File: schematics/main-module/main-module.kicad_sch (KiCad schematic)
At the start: 68 parts, among them J1 Conn_01x02_Socket, J3 Conn_01x04_Socket, J3 USB_C_Receptacle_USB2.0, J4 Conn_01x04_Pin, J5 Conn_01x02_Socket, J6 Conn_01x02_Pin, J7 FS1000A@433Mhz, J8 XY-MK-5V@433MHz, J9 AU-RM-5V@315мГц, M1 Creality 42-40, Q14 IRLML0030, Q7 BC847, SW1 KLS7-TS6601-7.0-180, SW2 SW_Push, U19 INA169, U2 CP2102N-Axx-xQFN28, U3 TMC2209_Module, U4 AMS1117-3.3, U8 ESP32-WROOM-32

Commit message: Creating schematics and boards
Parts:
- removed C18: 10 nF, Capacitor_SMD:C_0603_1608Metric, symbol Device:C
- removed C25 (x2): ?, Capacitor_SMD:C_0603_1608Metric, symbol Device:C
- removed J5: Conn_01x02_Socket, symbol Connector:Conn_01x02_Socket
- removed Q14 (x2): IRLML0030, Package_TO_SOT_SMD:SOT-23, symbol Transistor_FET:IRLML0030
- removed R15 (x2): 10K, Resistor_SMD:R_0805_2012Metric, symbol Device:R
- removed R52: 0.01, Resistor_SMD:R_2512_6332Metric, symbol Device:R
- removed R53: ?, Resistor_SMD:R_0805_2012Metric, symbol Device:R
- removed U19: INA169, Package_TO_SOT_SMD:SOT-23-5, symbol Amplifier_Current:INA169
- added C1: 1 uF, Capacitor_SMD:C_0603_1608Metric, symbol Device:C
- added C10 (x2): 1000 uF, symbol Device:C_Polarized
- added C10: 100 uF, symbol Device:C_Polarized
- added C11: 1000 uF, Capacitor_THT:CP_Radial_D8.0mm_P3.50mm, symbol Device:C_Polarized
- added C19 (x4): 22 uF, Capacitor_SMD:C_1210_3225Metric, symbol Device:C
- added C2: 400 pF, Capacitor_SMD:C_0603_1608Metric, symbol Device:C
- added C25: 1 nF, Capacitor_SMD:C_0603_1608Metric, symbol Device:C
- added C25: 10 uF, Capacitor_SMD:C_0603_1608Metric, symbol Device:C
- added C25: 500 nF, Capacitor_SMD:C_0603_1608Metric, symbol Device:C
- added C25 (x2), C26: 100 nF, Capacitor_SMD:C_0603_1608Metric, symbol Device:C
- added D2: HER508, Diode_THT:D_DO-201AD_P3.81mm_Vertical_AnodeUp, symbol Device:D
- added D3: US1M, Diode_SMD:D_SMA, symbol Device:D
- added D7: MB10S, Library:MBS, symbol Device:D_Bridge_+-AA
- added F1: 5A, symbol Device:Fuse
- added F1: 3A, symbol Device:Fuse
- added J3: Charger, symbol Connector:Conn_01x02_Socket
- added JP1: Charge from flusher, Library:SolderedJumper-2P-2mm, symbol Jumper:SolderJumper_2_Open
- added NT1: AGND/PGND, symbol Device:NetTie_2
- added Q1 (x2): IRF7832PbF, Package_SO:SOIC-8_3.9x4.9mm_P1.27mm, symbol Transistor_FET:IRF7403
- added Q14 (x2): IRLML0030, Package_TO_SOT_SMD:SOT-23, symbol Transistor_FET:IRLML0030
- added Q4: IRF7425PbF, Package_SO:SOIC-8_3.9x4.9mm_P1.27mm, symbol Transistor_FET:IRF7404
- added Q9: IRLML5203, Package_TO_SOT_SMD:SOT-23, symbol Transistor_FET:IRLML5203
- added R15 (x5): 10K, Resistor_SMD:R_0805_2012Metric, symbol Device:R
- added R15 (x4): 1K, Resistor_SMD:R_0805_2012Metric, symbol Device:R
- added R6: 50, 1W, symbol Device:R
- added RV1: 30K, symbol Device:R_Potentiometer
- added RV2: 1K, symbol Device:R_Potentiometer
- added T1: Transformer_1P_SS, symbol Device:Transformer_1P_SS
- added TP1, TP4: GND, symbol Connector:TestPoint
- added TP2: +5V, symbol Connector:TestPoint
- added TP3: +3V3, symbol Connector:TestPoint
- added TP5: VREF, symbol Connector:TestPoint
- added U3: AMS1117-5.0, Package_TO_SOT_SMD:SOT-223-3_TabPin2, symbol Regulator_Linear:AMS1117-5.0
- added U3: MC34063AD, Package_SO:SOP-8_3.9x4.9mm_P1.27mm, symbol Regulator_Switching:MC34063AD
- added U6: TL494, symbol Regulator_Controller:TL494
- added U7, U8: FAN3100, Package_TO_SOT_SMD:SOT-23-5, symbol My_Library:FAN3100
- J4: renamed from J7; value FS1000A@433Mhz -> STX882@433Mhz
- J5: renamed from J8; value XY-MK-5V@433MHz -> SRX882@433MHz
- J6: value Conn_01x02_Pin -> Power; now fitted
- L1: value L -> AMPLF0630, 8,2uH; now fitted
- R15: value 10K -> 1K
- renumbered D4 to D6, J9 to J7, J3 to J8, J4 to J9, U3 to U9
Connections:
- net +3V3: now also R15.1, TP3.1
- net +5V: now also C19.2, D3.1 (K), TP2.1, U3.2 (VO); no longer C10.1, C10.1, C19.2, C19.2, C29.1, C33.1, D5.2 (A2), J1.2 (Pin_2), J3.A4 (VBUS), J3.A9 (VBUS), J3.B4 (VBUS), J3.B9 (VBUS), R15.1, R15.1, U9.9 (VM)
- net GND1: now reaches D6.1 (K)
- net GND1: now also J6.2 (Pin_2), C10.2, C19.1, C19.1, C25.2, C25.2, C25.2, C25.2, D7.2 (-), Q1.1 (S), Q1.1 (S), Q1.2 (S), Q1.2 (S), Q1.3 (S), Q1.3 (S), R15.2, R15.2, RV2.3, TP4.1, U6.1 (1IN+), U6.10 (E2), U6.16 (2IN+), U6.7 (GND), U6.9 (E1), U7.2 (GND), U7.4 (IN-), U8.2 (GND), U8.4 (IN-)
- net at L1.1: now also D2.1 (K), Q4.5 (D), Q4.6 (D), Q4.7 (D), Q4.8 (D); no longer J6.1 (Pin_1)
- net VDC: now reaches L1.2
- net VDC: now also C10.1, C19.2, C19.2, U9.9 (VM), C11.1, RV1.1; no longer J6.2 (Pin_2)
- net VM_ENABLE: now reaches U8.10 (IO25)
- net VM_ENABLE: now also Q14.1 (G), R15.1
- net CHARGER_PING: no longer names the net of U8.6 (IO34)
- net CHARGER_PWM renamed CHARGER_ENABLE
- net CHARGER_ENABLE: now also Q14.1 (G), R15.1
- net CHARGER_START renamed CHARGER_START_BUTTON
- net CHARGER_START_BUTTON: now also C26.1, R15.2
- net GND renamed GNDA
- net GNDA: now also C1.1, C19.1, C19.1, C2.1, C26.2, NT1.2, Q14.2 (S), R15.2, RV1.3, TP1.1, U3.1 (GND), U3.4 (GND); no longer C10.2, C19.1, C19.1, J1.1 (Pin_1), U9.10 (GND), U9.16 (GND)
- new net: R15.2, U6.8 (C1), U7.3 (IN+)
- new net: Q1.4 (G), U7.5 (OUT)
- new net: C10.1, F1.2, J3.1 (Pin_1)
- new net: C10.2, J3.2 (Pin_2), Q14.3 (D)
- new net: R15.2, U6.11 (C2), U8.3 (IN+)
- new net: C25.1, U6.5 (CT)
- new net: R15.1, U6.6 (RT)
- new net: Q4.4 (G), R6.2, U3.1 (SwC), U3.8 (DC)
- new net: Q1.4 (G), U8.5 (OUT)
- new net: Q1.5 (D), Q1.6 (D), Q1.7 (D), Q1.8 (D), T1.3 (SA)
- new net: Q14.3 (D), Q9.1 (G), R15.2
- new net: C2.2, U3.3 (TC)
- new net: C25.1, D7.1 (+), RV2.1, TP5.1
- new net: Q1.5 (D), Q1.6 (D), Q1.7 (D), Q1.8 (D), T1.5 (SB)
- new net: D7.3, T1.1 (AA)
- new net: D7.4, T1.2 (AB)
- new net: D3.2 (A), JP1.2 (B)
- new net +7.5V: C19.2, F1.1, F1.2, Q4.1 (S), Q4.2 (S), Q4.3 (S), Q9.2 (S), R15.1, R6.1, U3.3 (VI)
- new net 7.5V_BEFORE_FUSE: C10.1, C10.1, C29.1, C33.1, F1.1, J1.2 (Pin_2)
- new net FB_VM: RV1.2, U3.5 (Vfb)
- new net GNDPWR: C10.2, C10.2, C11.2, C19.1, C19.1, D2.2 (A), J1.1 (Pin_1), NT1.1, Q14.2 (S), R15.2, U3.2 (SwE), U9.10 (GND), U9.16 (GND)
- new net TL494_DTC: C25.2, R15.1, R15.2, U6.4 (DTC)
- new net TL494_FEEDBACK: C25.1, RV2.2, U6.3 (FB)
- new net TL494_VREF: C25.1, R15.1, U6.13 (OUTCTRL), U6.14 (REF), U6.15 (2IN-), U6.2 (1IN-)
- new net VBUS: D5.2 (A2), J3.A4 (VBUS), J3.A9 (VBUS), J3.B4 (VBUS), J3.B9 (VBUS), JP1.1 (A), R15.1
- new net VD: C1.2, Q9.3 (D), U3.6 (Vin), U3.7 (Ipk)
- new net VPP: C10.1, C19.2, C19.2, C25.1, J6.1 (Pin_1), R15.1, R15.1, R15.1, T1.4 (SC), U6.12 (VCC), U7.1 (VCC), U8.1 (VCC)
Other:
- note added: "-----> WIRE ----->"
- note added: "80 KHz"
- note added: "Charger module (separated board)"
- note added: "TEST REQUIRED"
- moved on the sheet: C10, C18, C19, C25, C29, C33, D5, D6, J3, J4, J5, J7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

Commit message: Project prepared to order
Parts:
- removed C1: 1 uF, Capacitor_SMD:C_0603_1608Metric, symbol Device:C
- removed C10 (x3): 1000 uF, symbol Device:C_Polarized
- removed C10: 100 uF, symbol Device:C_Polarized
- removed C11: 1000 uF, Capacitor_THT:CP_Radial_D8.0mm_P3.50mm, symbol Device:C_Polarized
- removed C18 (x2): 10 nF, Capacitor_SMD:C_0603_1608Metric, symbol Device:C
- removed C19: 100 uF, Capacitor_SMD:C_0603_1608Metric, symbol Device:C
- removed C19 (x3): 22 uF, Capacitor_SMD:C_1210_3225Metric, symbol Device:C
- removed C2: 400 pF, Capacitor_SMD:C_0603_1608Metric, symbol Device:C
- removed D5 (x3): SMAJ26A, Diode_SMD:D_SMA, symbol Diode:ESD9B3.3ST5G
- removed J4: STX882@433Mhz, symbol Connector:Conn_01x03_Socket
- removed J5: SRX882@433MHz, symbol Connector:Conn_01x04_Socket
- removed J7: AU-RM-5V@315мГц, symbol Connector:Conn_01x04_Socket
- removed L1: AMPLF0630, 8,2uH, symbol Device:L
- removed Q9: IRLML5203, Package_TO_SOT_SMD:SOT-23, symbol Transistor_FET:IRLML5203
- removed R6: 50, 1W, symbol Device:R
- removed RV1: 30K, symbol Device:R_Potentiometer
- removed SW1: KLS7-TS6601-7.0-180, Button_Switch_THT:SW_PUSH_6mm_H5mm, symbol Switch:SW_Push
- removed SW2: SW_Push, symbol Switch:SW_Push
- removed U3: MC34063AD, Package_SO:SOP-8_3.9x4.9mm_P1.27mm, symbol Regulator_Switching:MC34063AD
- added C25: 0.1 uF, Capacitor_SMD:C_0603_1608Metric, symbol Device:C
- added C25 (x3): 100 nF, Capacitor_SMD:C_0603_1608Metric, symbol Device:C
- added C25: 10 uF, Capacitor_SMD:C_0603_1608Metric, symbol Device:C
- added C6 (x2): 100 uF, Capacitor_THT:CP_Radial_D6.3mm_P2.50mm, symbol Device:C_Polarized
- added D7: SMAJ5.0CA-TR, Diode_SMD:D_SMA, symbol Diode:ESD9B3.3ST5G
- added H1, H2, H3, H4: MountingHole, MountingHole:MountingHole_2.2mm_M2, symbol Mechanical:MountingHole
- added J5: Limit Switch, Connector_JST:JST_XH_B2B-XH-A_1x02_P2.50mm_Vertical, symbol Connector:Conn_01x02_Socket
- added R15: 10K, Resistor_SMD:R_0805_2012Metric, symbol Device:R
- added SW1 (x2): KLS7-TS3601-5.0-180, Library:SW_PUSH_P6.5_W3.5, symbol Switch:SW_Push
- added U10: SRX882@315Mhz, Library:SRX882_Vertical, symbol My_Library:SRX882
- added U6: SRX882@433Mhz, Library:SRX882_Vertical, symbol My_Library:SRX882
- added U7: STX882@433Mhz, Library:STX882_Vertical, symbol My_Library:STX882
- C10: footprint (none) -> Capacitor_THT:CP_Radial_D8.0mm_P3.50mm
- C25: value 0.1 uF -> 100 nF
- D5: renamed from D6; footprint (none) -> LED_THT:LED_D1.8mm_W3.3mm_H2.4mm
- F1: value 5A -> 6A; footprint (none) -> Library:FuseHolder1808
- F1: footprint (none) -> Library:FuseHolder1808
- J1, J3: footprint (none) -> Connector_JST:JST_XH_B2B-XH-A_1x02_P2.50mm_Vertical
- J4: renamed from J6; footprint (none) -> Connector_JST:JST_XH_B2B-XH-A_1x02_P2.50mm_Vertical
- J6: renamed from J8; footprint (none) -> Connector_JST:JST_XH_B4B-XH-A_1x04_P2.50mm_Vertical
- JP1: footprint Library:SolderedJumper-2P-2mm -> Jumper:SolderJumper-2_P1.3mm_Open_TrianglePad1.0x1.5mm
- NT1: footprint (none) -> NetTie:NetTie-2_SMD_Pad2.0mm
- RV2: footprint (none) -> Potentiometer_THT:Potentiometer_Runtron_RM-065_Vertical
- T1: footprint (none) -> Connector_JST:JST_XH_B5B-XH-A_1x05_P2.50mm_Vertical
- TP1: footprint (none) -> TestPoint:TestPoint_Plated_Hole_D2.0mm
- TP2, TP3: footprint (none) -> TestPoint:TestPoint_Pad_D1.0mm
- TP5: renamed from TP4; footprint (none) -> TestPoint:TestPoint_Plated_Hole_D2.0mm
- TP6: renamed from TP5; footprint (none) -> TestPoint:TestPoint_Pad_D1.0mm
- U13: renamed from U9; footprint https://www.trinamic.com/fileadmin/assets/Products/ICs_Documents/TMC2209_Datasheet_V103.pdf -> Library:TMC2209
- U9: renamed from U6; footprint (none) -> Package_SO:SO-16_3.9x9.9mm_P1.27mm
- renumbered D3 to D2, D7 to D6, J9 to J7, U7 to U11, U8 to U12
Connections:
- net VDC is gone; now on net VD: C19.2, C19.2, U13.9 (VM)
- net +3V3: now also C6.1, R15.1
- net +5V: now also C25.1, C25.1, C25.1, U10.3 (VCC), U10.4 (CS), U6.3 (VCC), U6.4 (CS), U7.3 (VCC)
- net CHARGER_ENABLE: now also U8.8 (IO32); no longer U8.26 (IO4)
- net CHARGER_START_BUTTON: now also SW1.1
- net ESP32_ENABLE: now also SW1.2
- net FM_IN_315: now also U8.33 (IO21); no longer U8.29 (IO5)
- net FM_IN_433: now also U8.29 (IO5); no longer U8.24 (IO2)
- net FM_IN_5V_315: now also U10.5 (DATA)
- net FM_IN_5V_433: now also U6.5 (DATA)
- net FM_OUT_433: now also U7.2 (DATA)
- net GND1: now also D2.2 (A), C25.2, C6.2; no longer U11.4 (IN-), U12.4 (IN-)
- net GNDA: now also C25.2, C25.2, C25.2, C25.2, C6.2, D7.1 (A1), J5.1 (Pin_1), SW1.1, SW1.2, U10.2 (GND), U10.6 (GND), U6.2 (GND), U6.6 (GND), U7.4 (GND)
- net GNDPWR: no longer D2.2 (A)
- net M_ENABLE#: now also U8.24 (IO2); no longer U8.33 (IO21)
- net TL494_VREF: now also C25.1
- net VBUS: now also D7.2 (A2)
- net VD: now also Q4.5 (D), Q4.6 (D), Q4.7 (D), Q4.8 (D)
- net VM_ENABLE: now also U8.14 (IO12); no longer U8.10 (IO25)
- net VPP: now also D2.1 (K), U11.3 (IN+), U12.3 (IN+), C6.1
- net at R15.2, U9.8 (C1): now also U11.4 (IN-); no longer U11.3 (IN+)
- net at R15.2, U9.11 (C2): now also U12.4 (IN-); no longer U12.3 (IN+)
- net at Q4.4 (G): now also Q14.3 (D), R15.2
- net at J7.1 (Pin_1): now also M1.1; no longer M1.2 (-)
- net at J7.2 (Pin_2): now also M1.2 (-); no longer M1.1
- net at U13.11 (M1B): now also J6.1 (Pin_1); no longer J6.2 (Pin_2)
- net at U13.12 (M1A): now also J6.2 (Pin_2); no longer J6.1 (Pin_1)
- new net LIMIT_SWITCH: C25.1, J5.2 (Pin_2), R15.2, U8.26 (IO4)
- no-connect marks 45 -> 44
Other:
- note added: "2A"
- note added: "5A"
- note removed: "80 KHz"
- note removed: "TEST REQUIRED"
- moved on the sheet: C19, C25, F1, J6, J7, M1, R15, U13, U8

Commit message: 1. start working under handle module; 2. rewrite stepper driver
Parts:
- C19: value 100 uF -> 4.7 uF
- C25: value 0.1 uF -> 330 nF
- C25: value 100 nF -> 4.7 uF
- C25: value 1 uF -> 330 nF
- C25: value 0.1 uF -> 4.7 uF
- C26: value 100 nF -> 330 nF
- C33: value 2.2 uF -> 4.7 uF
- R15: value 44K -> 47K
- R53: value 5K1 -> 22K
- R53: value 10K -> 47K
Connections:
- net RXD_3V3: now also U8.34 (RXD0/IO3); no longer U8.35 (TXD0/IO1)
- net TXD_3V3: now also U8.35 (TXD0/IO1); no longer U8.34 (RXD0/IO3)
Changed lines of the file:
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@@
     (stroke (width 0) (type default))
   )
-  (wire (pts (xy 359.41 96.52) (xy 384.81 96.52))
-    (stroke (width 0) (type default))
-  )
   (wire (pts (xy 90.17 288.29) (xy 105.41 288.29))
     (stroke (width 0) (type default))
@@
     (stroke (width 0) (type default))
   )
+  (wire (pts (xy 359.41 101.6) (xy 384.81 101.6))
+    (stroke (width 0) (type default))
+  )
   (wire (pts (xy 54.61 135.89) (xy 54.61 142.24))
     (stroke (width 0) (type default))
@@
     (stroke (width 0) (type default))
   )
+  (wire (pts (xy 359.41 96.52) (xy 384.81 96.52))
+    (stroke (width 0) (type default))
+  )
   (wire (pts (xy 330.2 250.19) (xy 330.2 252.73))
     (stroke (width 0) (type default))
@@
     (stroke (width 0) (type default))
   )
-  (wire (pts (xy 359.41 101.6) (xy 384.81 101.6))
-    (stroke (width 0) (type default))
-  )
   (wire (pts (xy 39.37 55.88) (xy 54.61 55.88))
     (stroke (width 0) (type default))
@@
     (effects (font (size 1.27 1.27)) (justify left))
   )
-  (hierarchical_label "TXD_3V3" (shape input) (at 384.81 101.6 0) (fields_autoplaced)
+  (hierarchical_label "TXD_3V3" (shape input) (at 384.81 96.52 0) (fields_autoplaced)
     (effects (font (size 1.27 1.27)) (justify left))
   )
@@
     (effects (font (size 1.27 1.27)) (justify left))
   )
-  (hierarchical_label "RXD_3V3" (shape input) (at 384.81 96.52 0) (fields_autoplaced)
+  (hierarchical_label "RXD_3V3" (shape input) (at 384.81 101.6 0) (fields_autoplaced)
     (effects (font (size 1.27 1.27)) (justify left))
   )
@@
       (effects (font (size 1.27 1.27)) (justify right))
     )
-    (property "Value" "5K1" (at 309.88 365.76 0)
+    (property "Value" "22K" (at 309.88 365.76 0)
       (effects (font (size 1.27 1.27)) (justify right))
     )
@@
       (effects (font (size 1.27 1.27)) (justify left))
     )
-    (property "Value" "2.2 uF" (at 27.94 60.96 0)
+    (property "Value" "4.7 uF" (at 27.94 60.96 0)
       (effects (font (size 1.27 1.27)) (justify left))
     )
@@
       (effects (font (size 1.27 1.27)) (justify left))
     )
-    (property "Value" "0.1 uF" (at 499.11 113.03 0)
+    (property "Value" "330 nF" (at 499.11 113.03 0)
       (effects (font (size 1.27 1.27)) (justify left))
     )
@@
       (effects (font (size 1.27 1.27)) (justify right))
     )
-    (property "Value" "10K" (at 309.88 377.19 0)
+    (property "Value" "47K" (at 309.88 377.19 0)
       (effects (font (size 1.27 1.27)) (justify right))
     )
@@
       (effects (font (size 1.27 1.27)) (justify left))
     )
-    (property "Value" "100 nF" (at 219.71 372.11 0)
+    (property "Value" "4.7 uF" (at 219.71 372.11 0)
       (effects (font (size 1.27 1.27)) (justify left))
     )
@@
       (effects (font (size 1.27 1.27)) (justify left))
     )
-    (property "Value" "100 nF" (at 387.35 66.04 0)
+    (property "Value" "4.7 uF" (at 387.35 66.04 0)
       (effects (font (size 1.27 1.27)) (justify left))
     )
@@
       (effects (font (size 1.27 1.27)))
     )
-    (property "Value" "44K" (at 31.75 336.55 0)
+    (property "Value" "47K" (at 31.75 336.55 0)
       (effects (font (size 1.27 1.27)))
     )
@@
       (effects (font (size 1.27 1.27)) (justify right))
     )
-    (property "Value" "5K1" (at 426.72 369.57 0)
+    (property "Value" "22K" (at 426.72 369.57 0)
       (effects (font (size 1.27 1.27)) (justify right))
     )
@@
       (effects (font (size 1.27 1.27)) (justify left))
     )
-    (property "Value" "1 uF" (at 302.26 101.6 0)
+    (property "Value" "330 nF" (at 302.26 101.6 0)
       (effects (font (size 1.27 1.27)) (justify left))
     )
@@
       (effects (font (size 1.27 1.27)) (justify left))
     )
-    (property "Value" "100 nF" (at 219.71 337.82 0)
+    (property "Value" "4.7 uF" (at 219.71 337.82 0)
       (effects (font (size 1.27 1.27)) (justify left))
     )
@@
       (effects (font (size 1.27 1.27)) (justify right))
     )
-    (property "Value" "100 uF" (at 217.17 116.84 0)
+    (property "Value" "4.7 uF" (at 217.17 116.84 0)
       (effects (font (size 1.27 1.27)) (justify right))
     )
@@
       (effects (font (size 1.27 1.27)) (justify left))
     )
-    (property "Value" "100 nF" (at 542.29 44.45 0)
+    (property "Value" "330 nF" (at 542.29 44.45 0)
       (effects (font (size 1.27 1.27)) (justify left))
     )
@@
       (effects (font (size 1.27 1.27)) (justify left))
     )
-    (property "Value" "0.1 uF" (at 146.05 106.68 0)
+    (property "Value" "4.7 uF" (at 146.05 106.68 0)
       (effects (font (size 1.27 1.27)) (justify left))
     )
@@
       (effects (font (size 1.27 1.27)) (justify left))
     )
-    (property "Value" "100 nF" (at 353.06 378.46 0)
+    (property "Value" "4.7 uF" (at 353.06 378.46 0)
       (effects (font (size 1.27 1.27)) (justify left))
     )
@@
       (effects (font (size 1.27 1.27)) (justify right))
     )
-    (property "Value" "10K" (at 426.72 381 0)
+    (property "Value" "47K" (at 426.72 381 0)
       (effects (font (size 1.27 1.27)) (justify right))
     )

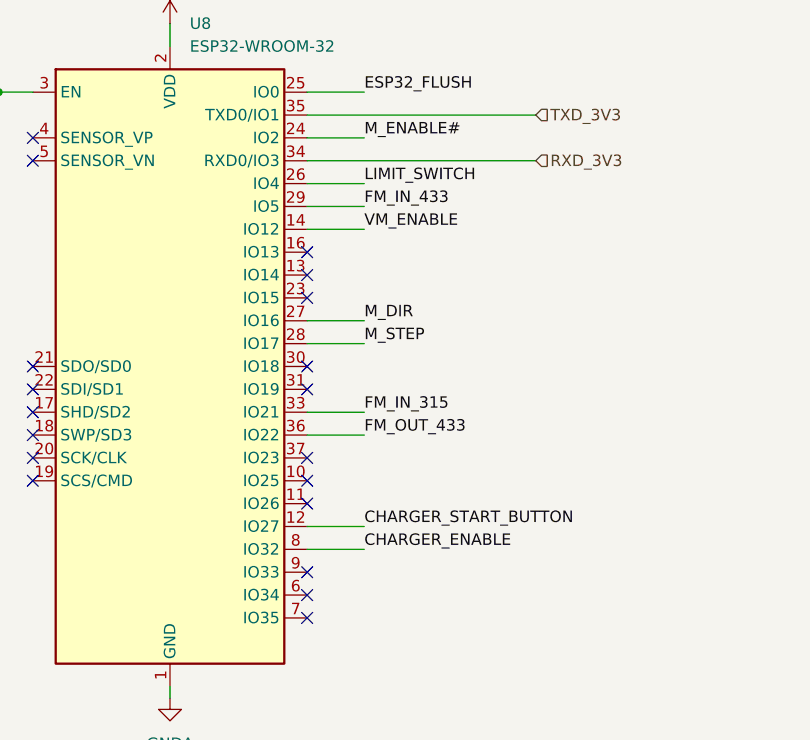
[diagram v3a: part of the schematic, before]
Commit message: 1. Fixed schema - limit switch connection moved to ADC pin
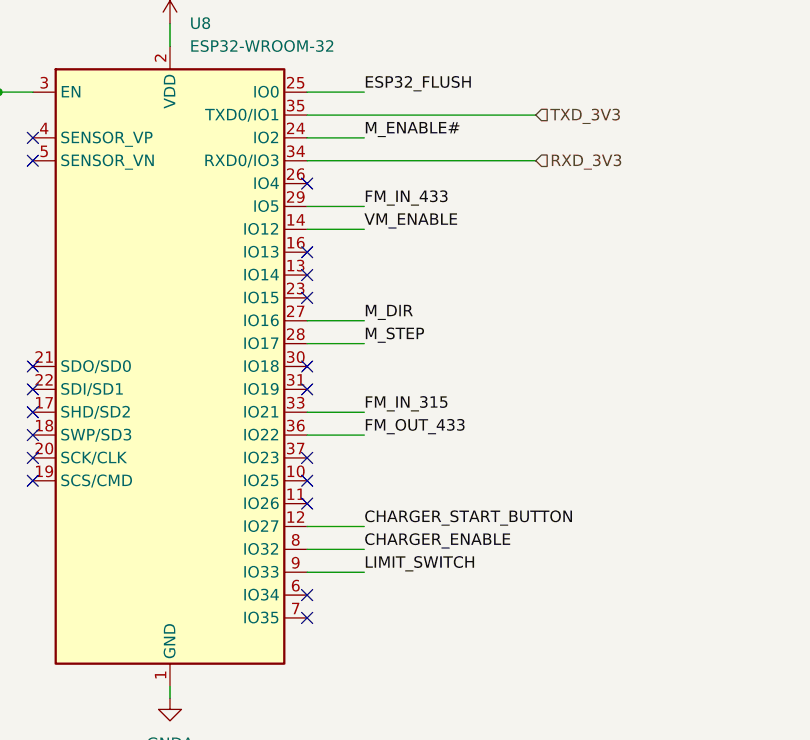
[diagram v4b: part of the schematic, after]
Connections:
- net LIMIT_SWITCH: now also U8.9 (IO33); no longer U8.26 (IO4)
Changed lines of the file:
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@@
   (no_connect (at 93.98 349.25))
   (no_connect (at 93.98 367.03))
-  (no_connect (at 359.41 147.32))
   (no_connect (at 359.41 149.86))
   (no_connect (at 93.98 359.41))
@@
   (no_connect (at 63.5 213.36))
   (no_connect (at 328.93 99.06))
+  (no_connect (at 359.41 104.14))
   (no_connect (at 328.93 127))
   (no_connect (at 359.41 116.84))
@@
     (stroke (width 0) (type default))
   )
+  (wire (pts (xy 359.41 147.32) (xy 365.76 147.32))
+    (stroke (width 0) (type default))
+  )
   (wire (pts (xy 165.1 173.99) (xy 165.1 176.53))
     (stroke (width 0) (type default))
@@
   )
   (wire (pts (xy 508 242.57) (xy 508 241.3))
-    (stroke (width 0) (type default))
-  )
-  (wire (pts (xy 359.41 104.14) (xy 365.76 104.14))
     (stroke (width 0) (type default))
   )
@@
     (effects (font (size 1.27 1.27)) (justify left bottom))
   )
-  (label "LIMIT_SWITCH" (at 365.76 104.14 0) (fields_autoplaced)
-    (effects (font (size 1.27 1.27)) (justify left bottom))
-  )
+  (label "LIMIT_SWITCH" (at 365.76 147.32 0) (fields_autoplaced)
+    (effects (font (size 1.27 1.27)) (justify left bottom))
+  )

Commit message: 3d models
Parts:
- added J8: Conn_01x02_Pin, symbol Connector:Conn_01x02_Pin
- added R15: 33K, Resistor_SMD:R_0805_2012Metric, symbol Device:R
- added R15: 7K5, Resistor_SMD:R_0805_2012Metric, symbol Device:R
- added SW3, SW4: Limit Switch, symbol Switch:SW_Push
- added SW6: Limit Switch, symbol Switch:SW_Push_Open
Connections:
- new net: J8.2 (Pin_2), SW3.2, SW4.2, SW6.1 (A)
- new net: J8.1 (Pin_1), R15.1, R15.1, SW6.2 (B)
- new net: R15.2, SW4.1
- new net: R15.2, SW3.1
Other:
- moved on the sheet: C25, J5, R15

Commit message: Working under firmware
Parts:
- R15: value 33K -> 20K
- R15: value 7K5 -> 3K
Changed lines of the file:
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@@
       (effects (font (size 1.27 1.27)))
     )
-    (property "Value" "33K" (at 483.87 111.76 0)
+    (property "Value" "20K" (at 483.87 111.76 0)
       (effects (font (size 1.27 1.27)))
     )
@@
       (effects (font (size 1.27 1.27)))
     )
-    (property "Value" "7K5" (at 496.57 111.76 0)
+    (property "Value" "3K" (at 496.57 111.76 0)
       (effects (font (size 1.27 1.27)))
     )
